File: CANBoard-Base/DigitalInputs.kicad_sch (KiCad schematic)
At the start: 18 parts, among them U6 SRV05-4, U7 SRV05-4

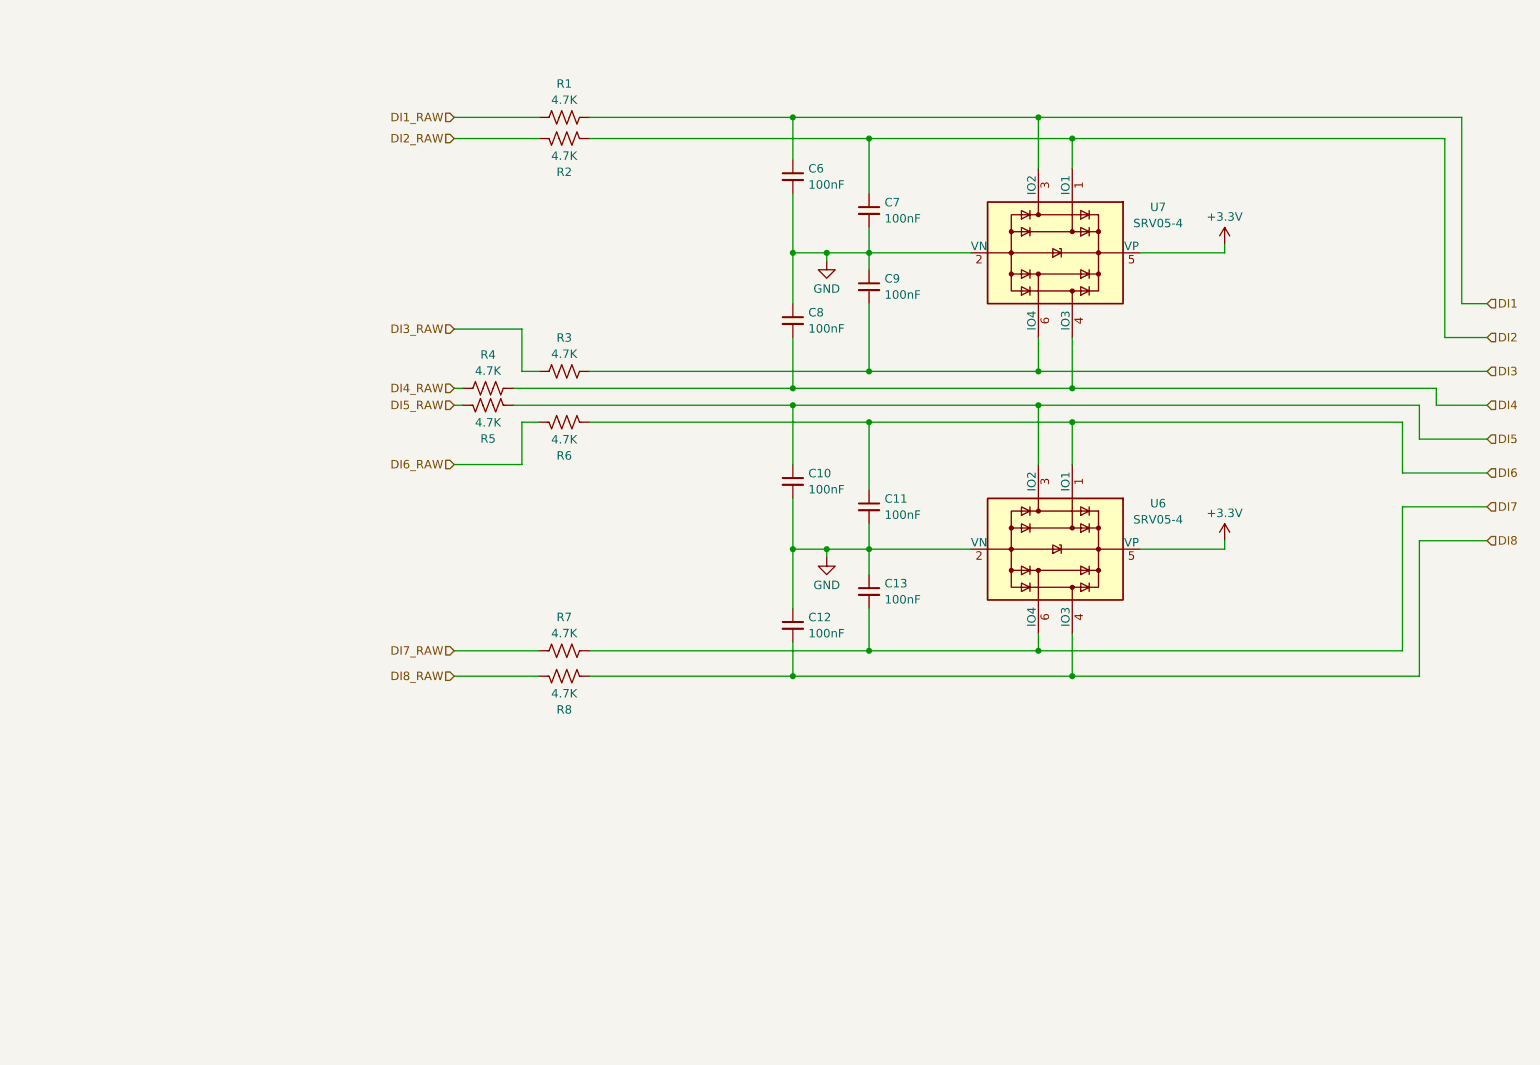
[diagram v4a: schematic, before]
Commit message: moved dtm connectors together
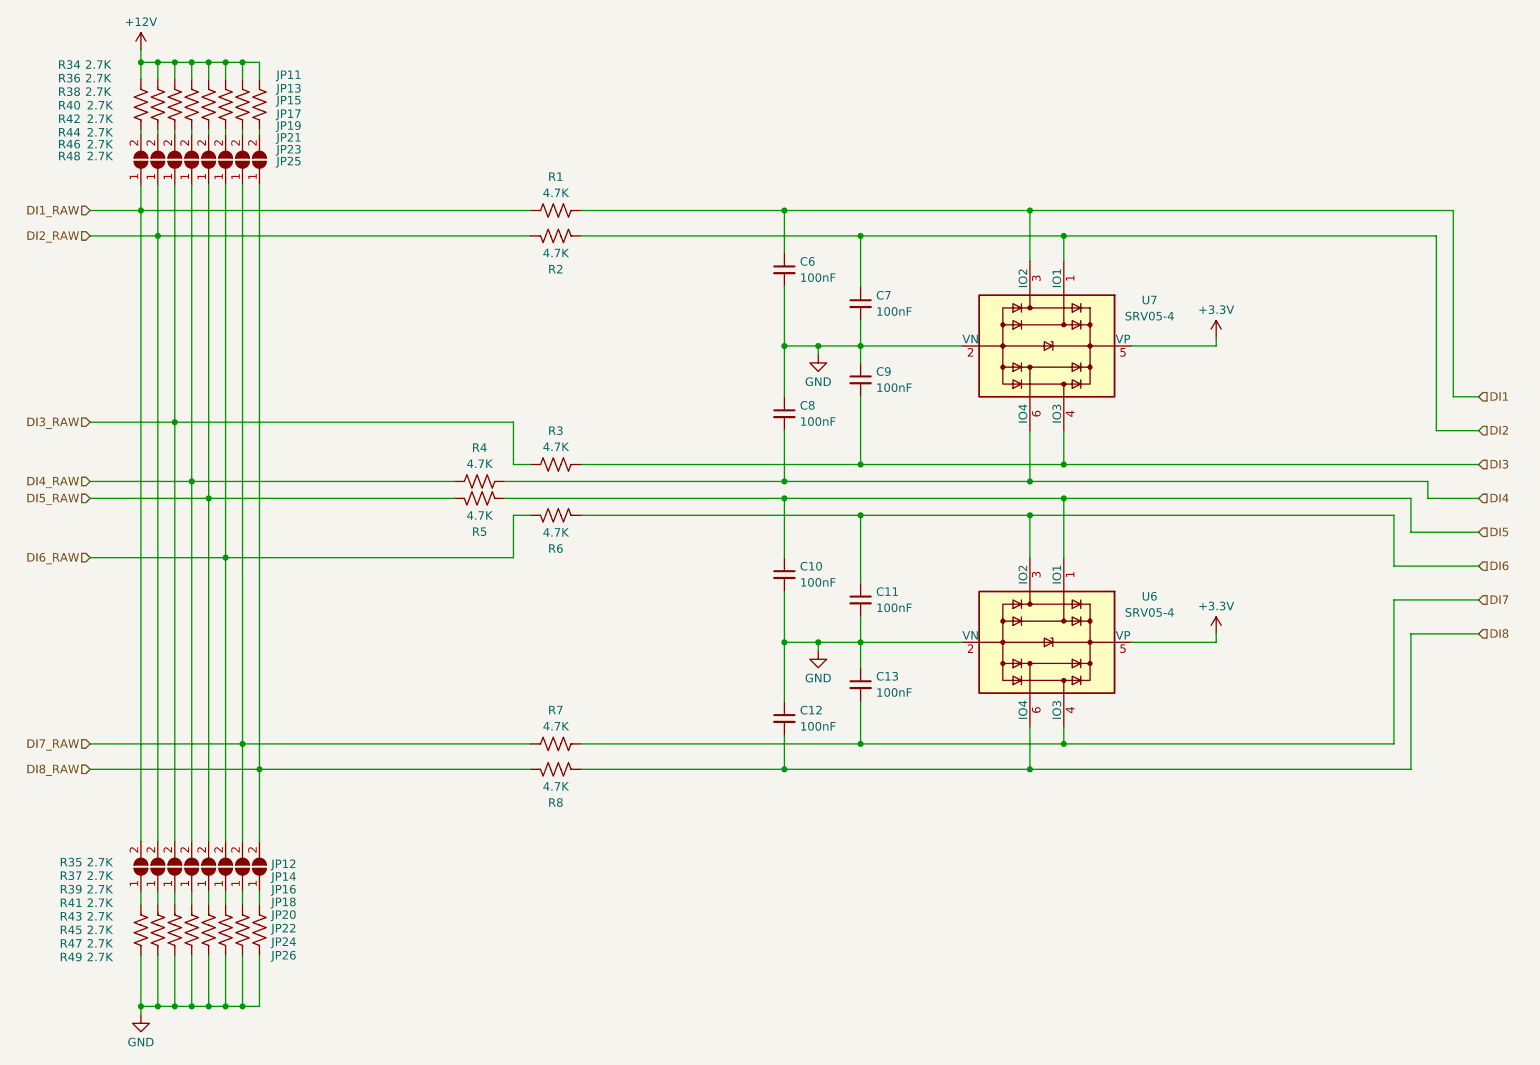
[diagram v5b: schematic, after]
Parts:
- added JP11, JP12, JP13, JP14, JP15, JP16, JP17, JP18, JP19, JP20, JP21, JP22, JP23, JP24, JP25, JP26: SolderJumper_2_Open, Jumper:SolderJumper-2_P1.3mm_Open_RoundedPad1.0x1.5mm, symbol Jumper:SolderJumper_2_Open
- added R34, R35, R36, R37, R38, R39, R40, R41, R42, R43, R44, R45, R46, R47, R48, R49: 2.7K, Resistor_SMD:R_0805_2012Metric, symbol Device:R_US
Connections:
- net DI1_RAW: now also JP11.1 (A), JP12.2 (B)
- net DI2_RAW: now also JP13.1 (A), JP14.2 (B)
- net DI3: now also U7.4 (IO3); no longer U7.6 (IO4)
- net DI3_RAW: now also JP15.1 (A), JP16.2 (B)
- net DI4: now also U7.6 (IO4); no longer U7.4 (IO3)
- net DI4_RAW: now also JP17.1 (A), JP18.2 (B)
- net DI5: now also U6.1 (IO1); no longer U6.3 (IO2)
- net DI5_RAW: now also JP19.1 (A), JP20.2 (B)
- net DI6: now also U6.3 (IO2); no longer U6.1 (IO1)
- net DI6_RAW: now also JP21.1 (A), JP22.2 (B)
- net DI7: now also U6.4 (IO3); no longer U6.6 (IO4)
- net DI7_RAW: now also JP23.1 (A), JP24.2 (B)
- net DI8: now also U6.6 (IO4); no longer U6.4 (IO3)
- net DI8_RAW: now also JP25.1 (A), JP26.2 (B)
- net GND: now also R35.2, R37.2, R39.2, R41.2, R43.2, R45.2, R47.2, R49.2
- new net: JP25.2 (B), R48.2
- new net: JP24.1 (A), R47.1
- new net: JP26.1 (A), R49.1
- new net: JP17.2 (B), R40.2
- new net: JP16.1 (A), R39.1
- new net: JP13.2 (B), R36.2
- new net: JP19.2 (B), R42.2
- new net: JP22.1 (A), R45.1
- new net: JP11.2 (B), R34.2
- new net: JP21.2 (B), R44.2
- new net: JP15.2 (B), R38.2
- new net: JP18.1 (A), R41.1
- new net: JP20.1 (A), R43.1
- new net: JP14.1 (A), R37.1
- new net: JP12.1 (A), R35.1
- new net: JP23.2 (B), R46.2
- new net +12V: R34.1, R36.1, R38.1, R40.1, R42.1, R44.1, R46.1, R48.1
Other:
- moved on the sheet: C10, C11, C12, C13, C6, C7, C8, C9, R1, R2, R3, R4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
